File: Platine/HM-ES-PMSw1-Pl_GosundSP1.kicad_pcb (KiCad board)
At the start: 2 copper layers, 23.2 x 20.7 mm, 11 parts, among them J1 Conn_BW-SHP2, U1 ATMEGA644PA-AU, U2 CC1101

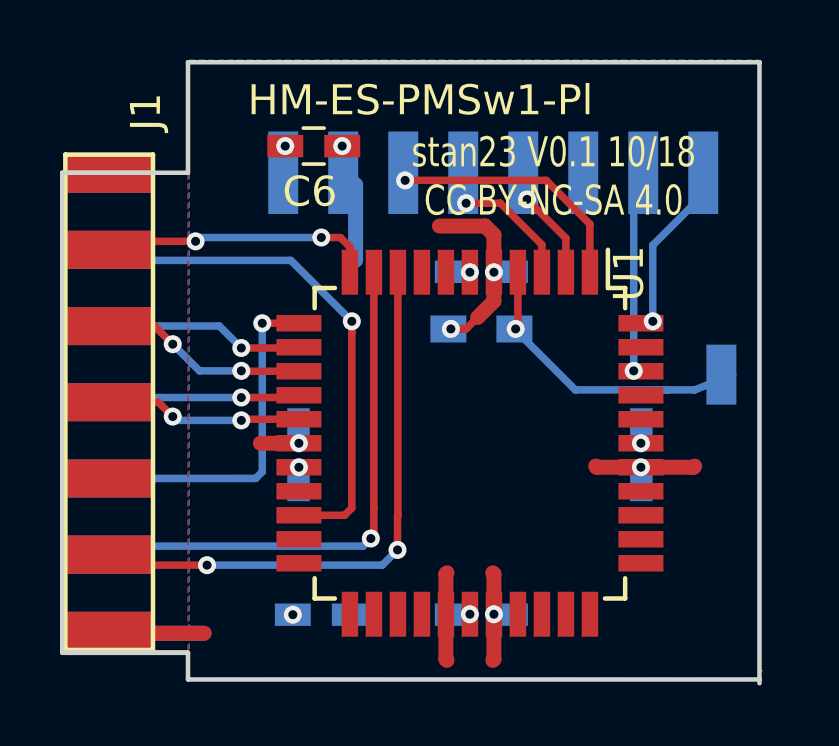
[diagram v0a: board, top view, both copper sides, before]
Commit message: fix wrong Paste layer in connetor
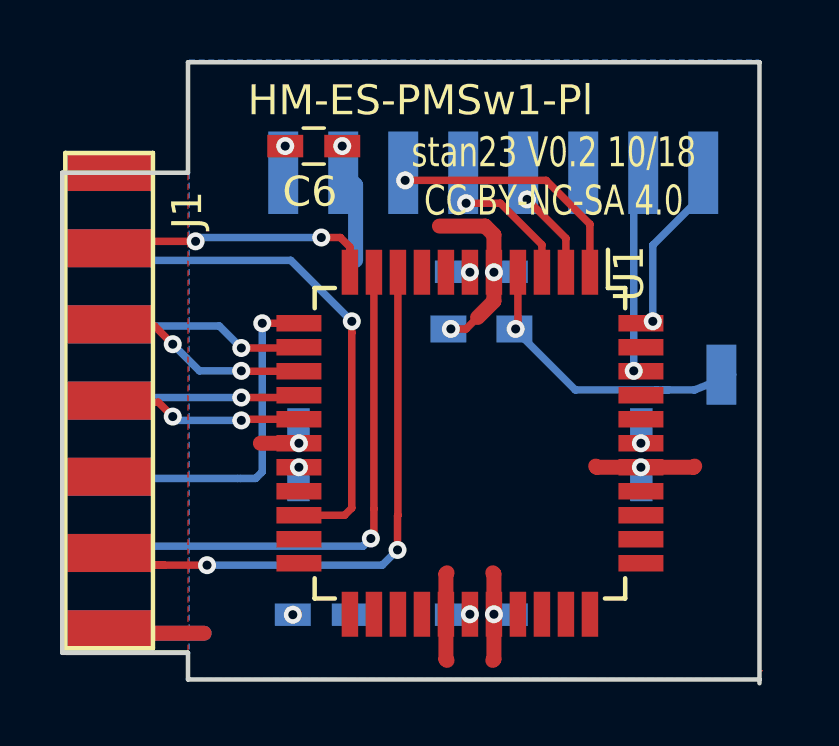
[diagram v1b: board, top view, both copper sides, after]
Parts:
- moved J1 0.06 mm to (97.9, 102.2)
- renumbered Reset to J4
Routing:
- net /RX: track 19.7 -> 21.7 mm
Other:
- board text added: "stan23 V0.2 10/18 CC BY-NC-SA 4.0"
- board text removed: "stan23 V0.1 10/18 CC BY-NC-SA 4.0"

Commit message: add resonator for better clock
e.g. CSTCE8M00G55-R0, available at Reichelt (CSTCE 8,00)
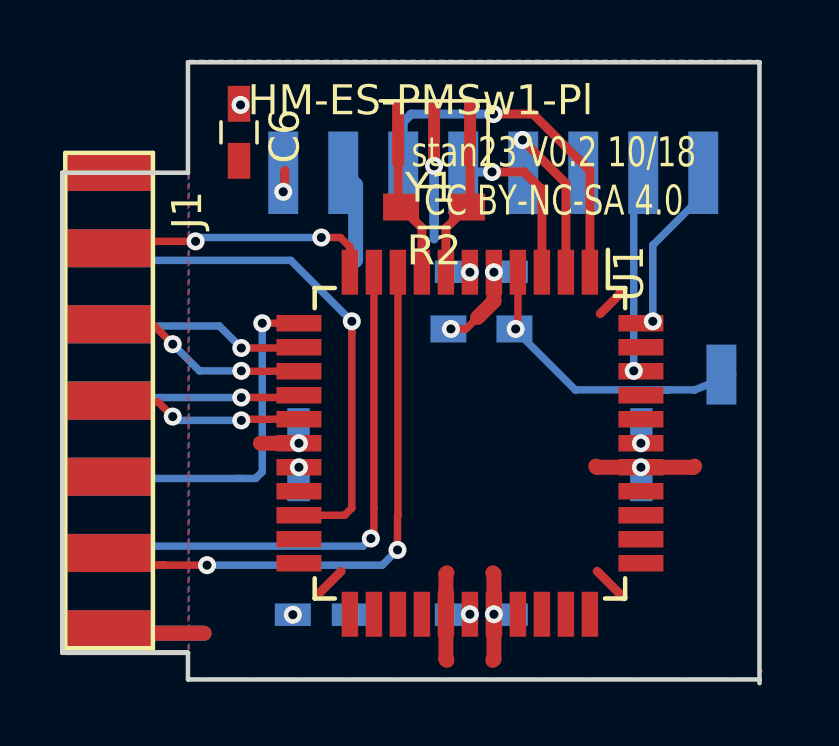
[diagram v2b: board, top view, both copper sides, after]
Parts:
- added R2: 1M, Resistors_SMD:R_0603_HandSoldering, F.Cu at (108.7, 95.8)
- added Y1: Resonator, Resonators:Resonator_SMD_muRata_TPSKA-3pin_7.9x3.8mm_HandSoldering, F.Cu at (108.7, 93.3)
- moved C6 2.53 mm to (102.2, 93.3), turned to 90 degrees
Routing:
- net GND: track 9.96 -> 15.5 mm, vias 5 -> 6
- net Net-(R2-Pad1): track 0.00 -> 4.95 mm
- net Net-(R2-Pad2): track 0.00 -> 4.94 mm
- net /MOSI: track 8.71 -> 12.5 mm
- net (no net): track 0.00 -> 3.28 mm
- net /MISO: track 4.44 -> 7.41 mm
- net /SCK: track 6.31 -> 8.93 mm
- net VCC: track 23.6 -> 22.9 mm

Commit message: finalize V1.0
fix #1, #2, #4
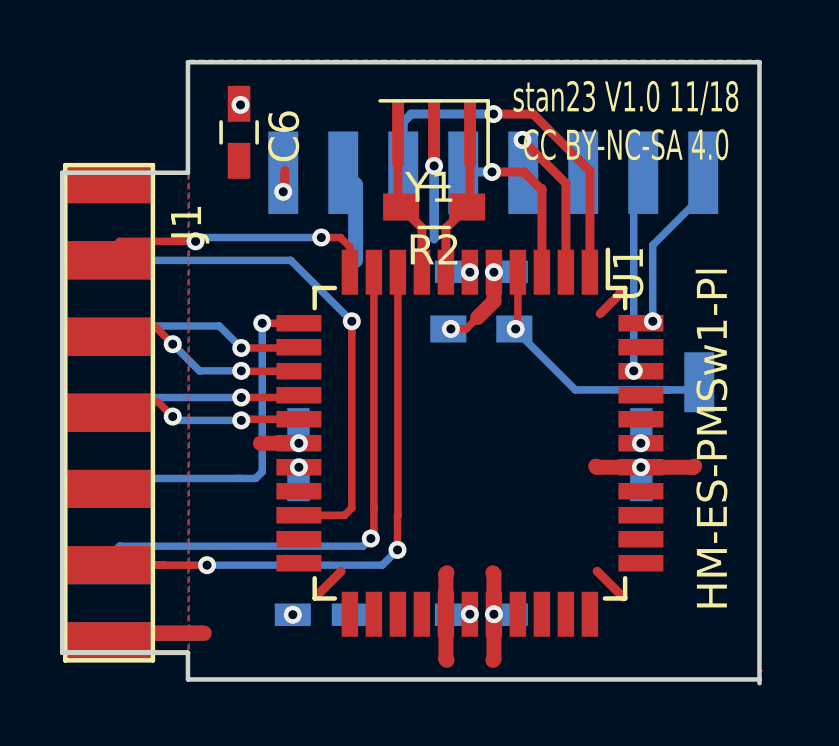
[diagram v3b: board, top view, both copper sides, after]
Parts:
- removed J4: Reset, SMD_Packages:1Pin
- added Reset: Reset, Testpads:Testpad, B.Cu at (117.5, 101.6)
- moved J1 0.41 mm to (97.9, 102.6)
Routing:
- net /RESET: track 10.3 -> 9.54 mm
- net /RX: track 21.7 -> 21.1 mm
- net /CF1: track 9.68 -> 9.10 mm
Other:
- board text added: "VCC GND MOSI SCK MISO GDO0 CS"
- board text added: "stan23 V1.0 11/18 CC BY-NC-SA 4.0"
- board text removed: "stan23 V0.2 10/18 CC BY-NC-SA 4.0"
